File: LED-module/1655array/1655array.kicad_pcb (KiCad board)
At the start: 2 copper layers, 26 x 93 mm, 44 parts, among them J1 Conn_01x04, J2 Conn_02x02_Counter_Clockwise, J3 Conn_02x02_Counter_Clockwise, J4 Conn_02x02_Counter_Clockwise, J5 Conn_02x02_Counter_Clockwise

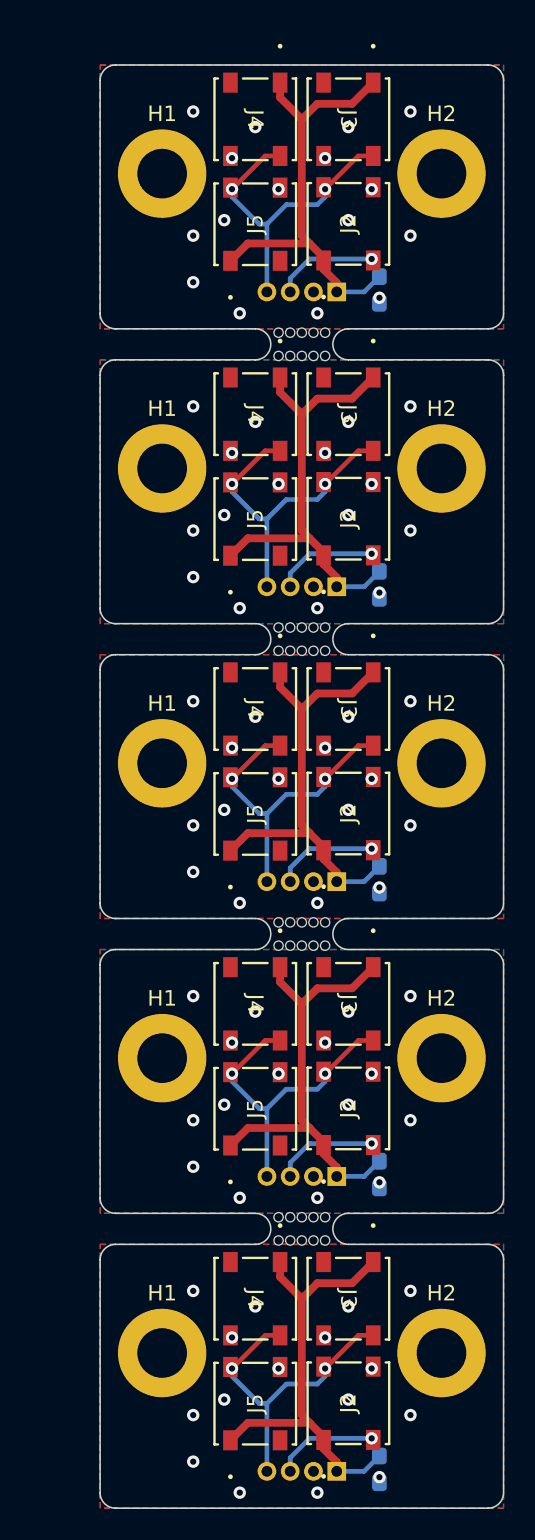
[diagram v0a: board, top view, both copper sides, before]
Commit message: add clearance
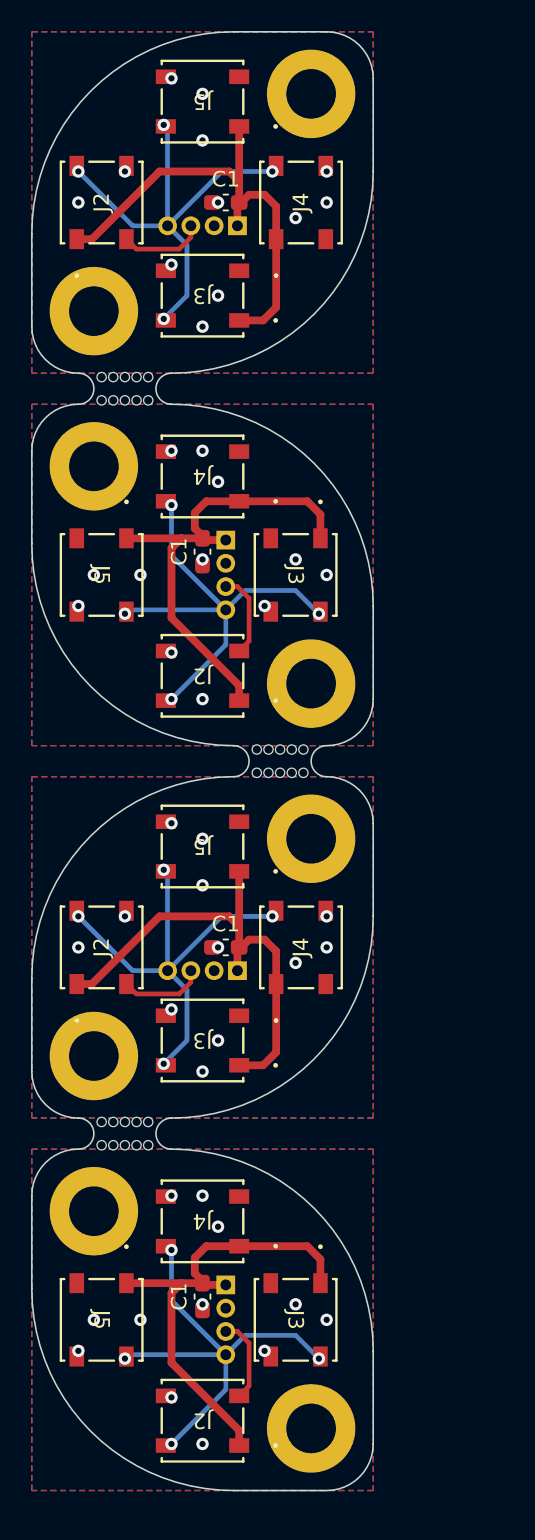
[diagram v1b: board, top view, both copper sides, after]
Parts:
- removed the C1 at (161.4, 147.6)
- removed the C1 at (161.4, 71.6)
- removed the C1 at (161.4, 109.6)
- removed the C1 at (161.4, 90.6)
- removed the C1 at (161.4, 128.6)
- removed the H1 at (147.4, 140.1)
- removed the H1 at (147.4, 102.1)
- removed the H1 at (147.4, 64.1)
- removed the H1 at (147.4, 121.1)
- removed the H1 at (147.4, 83.1)
- removed the H2 at (165.4, 121.1)
- removed the H2 at (165.4, 83.1)
- removed the H2 at (165.4, 140.1)
- removed the H2 at (165.4, 64.1)
- removed the H2 at (165.4, 102.1)
- removed the J1 at (156.4, 90.8)
- removed the J1 at (156.4, 71.8)
- removed the J1 at (156.4, 109.8)
- removed the J1 at (156.4, 128.8)
- removed the J1 at (156.4, 147.8)
- removed the J2 at (159.4, 86.4)
- removed the J2 at (159.4, 67.4)
- removed the J2 at (159.4, 143.4)
- removed the J2 at (159.4, 124.4)
- removed the J2 at (159.4, 105.4)
- removed the J3 at (159.4, 98.6)
- removed the J3 at (159.4, 117.6)
- removed the J3 at (159.4, 79.6)
- removed the J3 at (159.4, 136.6)
- removed the J3 at (159.4, 60.6)
- removed the J4 at (153.4, 117.6)
- removed the J4 at (153.4, 136.6)
- removed the J4 at (153.4, 98.6)
- removed the J4 at (153.4, 60.6)
- removed the J4 at (153.4, 79.6)
- removed the J5 at (153.4, 86.4)
- removed the J5 at (153.4, 105.4)
- removed the J5 at (153.4, 143.4)
- removed the J5 at (153.4, 67.4)
- removed the J5 at (153.4, 124.4)
- removed the REF** at (153.4, 95.1)
- removed the REF** at (153.4, 114.1)
- removed the REF** at (153.4, 133.1)
- removed the REF** at (153.4, 76.1)
- added C1: C, Capacitor_SMD:C_0603_1608Metric_Pad1.08x0.95mm_HandSolder, F.Cu at (150.0, 136.5)
- added C1: C, Capacitor_SMD:C_0603_1608Metric_Pad1.08x0.95mm_HandSolder, F.Cu at (150.0, 88.5)
- added C1: C, Capacitor_SMD:C_0603_1608Metric_Pad1.08x0.95mm_HandSolder, F.Cu at (151.5, 66.0)
- added C1: C, Capacitor_SMD:C_0603_1608Metric_Pad1.08x0.95mm_HandSolder, F.Cu at (151.5, 114.0)
- added H1: MountingHole, MountingHole:MountingHole_3.2mm_M3_ISO7380_Pad, F.Cu at (157.0, 145.0)
- added H1: MountingHole, MountingHole:MountingHole_3.2mm_M3_ISO7380_Pad, F.Cu at (143.0, 121.0)
- added H1: MountingHole, MountingHole:MountingHole_3.2mm_M3_ISO7380_Pad, F.Cu at (143.0, 73.0)
- added H1: MountingHole, MountingHole:MountingHole_3.2mm_M3_ISO7380_Pad, F.Cu at (157.0, 97.0)
- added H2: MountingHole, MountingHole:MountingHole_3.2mm_M3_ISO7380_Pad, F.Cu at (143.0, 131.0)
- added H2: MountingHole, MountingHole:MountingHole_3.2mm_M3_ISO7380_Pad, F.Cu at (157.0, 107.0)
- added H2: MountingHole, MountingHole:MountingHole_3.2mm_M3_ISO7380_Pad, F.Cu at (143.0, 83.0)
- added H2: MountingHole, MountingHole:MountingHole_3.2mm_M3_ISO7380_Pad, F.Cu at (157.0, 59.0)
- added J1: Conn_01x04, LED-module:JST_S4B-ZR_LF__SN_, B.Cu at (150.0, 67.5)
- added J1: Conn_01x04, LED-module:JST_S4B-ZR_LF__SN_, B.Cu at (151.5, 90.0)
- added J1: Conn_01x04, LED-module:JST_S4B-ZR_LF__SN_, B.Cu at (151.5, 138.0)
- added J1: Conn_01x04, LED-module:JST_S4B-ZR_LF__SN_, B.Cu at (150.0, 115.5)
- added J2: Conn_02x02_Counter_Clockwise, LED-module:LED_2758_ADA, F.Cu at (143.5, 114.0)
- added J2: Conn_02x02_Counter_Clockwise, LED-module:LED_2758_ADA, F.Cu at (143.5, 66.0)
- added J2: Conn_02x02_Counter_Clockwise, LED-module:LED_2758_ADA, F.Cu at (150.0, 144.5)
- added J2: Conn_02x02_Counter_Clockwise, LED-module:LED_2758_ADA, F.Cu at (150.0, 96.5)
- added J3: Conn_02x02_Counter_Clockwise, LED-module:LED_2758_ADA, F.Cu at (156.0, 138.0)
- added J3: Conn_02x02_Counter_Clockwise, LED-module:LED_2758_ADA, F.Cu at (156.0, 90.0)
- added J3: Conn_02x02_Counter_Clockwise, LED-module:LED_2758_ADA, F.Cu at (150.0, 72.0)
- added J3: Conn_02x02_Counter_Clockwise, LED-module:LED_2758_ADA, F.Cu at (150.0, 120.0)
- added J4: Conn_02x02_Counter_Clockwise, LED-module:LED_2758_ADA, F.Cu at (156.3, 66.0)
- added J4: Conn_02x02_Counter_Clockwise, LED-module:LED_2758_ADA, F.Cu at (156.3, 114.0)
- added J4: Conn_02x02_Counter_Clockwise, LED-module:LED_2758_ADA, F.Cu at (150.0, 131.7)
- added J4: Conn_02x02_Counter_Clockwise, LED-module:LED_2758_ADA, F.Cu at (150.0, 83.7)
- added J5: Conn_02x02_Counter_Clockwise, LED-module:LED_2758_ADA, F.Cu at (150.0, 59.5)
- added J5: Conn_02x02_Counter_Clockwise, LED-module:LED_2758_ADA, F.Cu at (143.5, 138.0)
- added J5: Conn_02x02_Counter_Clockwise, LED-module:LED_2758_ADA, F.Cu at (143.5, 90.0)
- added J5: Conn_02x02_Counter_Clockwise, LED-module:LED_2758_ADA, F.Cu at (150.0, 107.5)
- added REF**: stamphole_2x5, LED-module:stamphole_2x5, F.Cu at (142.0, 79.0)
- added REF**: stamphole_2x5, LED-module:stamphole_2x5, F.Cu at (148.0, 125.0)
- added REF**: stamphole_2x5, LED-module:stamphole_2x5, F.Cu at (152.0, 103.0)
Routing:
- net +5V: track 146.5 -> 124.5 mm
- net /DIN: track 104.0 -> 116.6 mm, vias 10 -> 16
- net /DOUT: track 33.2 -> 21.9 mm, vias 5 -> 0
- net GND: vias 80 -> 48
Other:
- board size 26 x 93 mm -> 22 x 94 mm
- board text added: "MountingHole"

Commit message: expand
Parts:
- removed the C1 at (150.0, 136.5)
- removed the C1 at (150.0, 88.5)
- removed the C1 at (151.5, 114.0)
- removed the H1 at (157.0, 145.0)
- removed the H1 at (143.0, 121.0)
- removed the H1 at (157.0, 97.0)
- removed the H2 at (143.0, 131.0)
- removed the H2 at (157.0, 107.0)
- removed the H2 at (143.0, 83.0)
- removed the J1 at (151.5, 90.0)
- removed the J1 at (151.5, 138.0)
- removed the J1 at (150.0, 115.5)
- removed the J2 at (143.5, 114.0)
- removed the J2 at (150.0, 144.5)
- removed the J2 at (150.0, 96.5)
- removed the J3 at (156.0, 138.0)
- removed the J3 at (156.0, 90.0)
- removed the J3 at (150.0, 120.0)
- removed the J4 at (156.3, 114.0)
- removed the J4 at (150.0, 131.7)
- removed the J4 at (150.0, 83.7)
- removed the J5 at (143.5, 138.0)
- removed the J5 at (143.5, 90.0)
- removed the J5 at (150.0, 107.5)
- removed REF** (x3): stamphole_2x5, LED-module:stamphole_2x5
- added C1: C, Capacitor_SMD:C_0603_1608Metric_Pad1.08x0.95mm_HandSolder, F.Cu at (208.5, 69.8)
- added H1: MountingHole, MountingHole:MountingHole_3.2mm_M3_ISO7380_Pad, F.Cu at (202.5, 62.5)
- added H2: MountingHole, MountingHole:MountingHole_3.2mm_M3_ISO7380_Pad, F.Cu at (217.5, 76.5)
- added J1: Conn_01x04, LED-module:JST_S4B-ZR_LF__SN_, B.Cu at (210.0, 67.9)
- added J2: Conn_02x02_Counter_Clockwise, LED-module:LED_2758_ADA, F.Cu at (220.0, 69.5)
- added J3: Conn_02x02_Counter_Clockwise, LED-module:LED_2758_ADA, F.Cu at (210.0, 59.5)
- added J4: Conn_02x02_Counter_Clockwise, LED-module:LED_2758_ADA, F.Cu at (200.0, 69.5)
- added J5: Conn_02x02_Counter_Clockwise, LED-module:LED_2758_ADA, F.Cu at (210.0, 79.5)
- moved H1 46.4 mm to (189.0, 79.0)
- moved J4 36.4 mm to (192.5, 70.0), turned to -90 degrees
- moved J3 31.8 mm to (180.0, 82.5)
- moved J1 30.3 mm to (180.0, 71.6)
- moved C1 30.2 mm to (181.5, 69.8)
- moved J5 30.1 mm to (180.0, 57.5), turned to 0 degrees
- moved J2 24.3 mm to (167.5, 70.0)
- moved H2 14.1 mm to (171.0, 61.0)
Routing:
- net (no net): track 0.00 -> 2.66 mm
- net /DOUT: track 21.9 -> 19.5 mm
- net +5V: track 124.5 -> 122.5 mm
- net /DIN: track 116.6 -> 116.2 mm, vias 16 -> 8
- net GND: vias 48 -> 36
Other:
- board size 22 x 94 mm -> 59.5 x 32 mm
- board text removed: "MountingHole"
